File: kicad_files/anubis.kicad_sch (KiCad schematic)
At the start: 261 parts, among them J1 A1001WR-S-04P, J2 A1001WR-S-04P, J3 Conn_01x06, Q1 AO3401A, Q2 2N7002, Q3 DTC123JKAT146, Q4 DTC123JKAT146, Q5 DTC123JKAT146, Q6 DTC123JKAT146, SW1 K2-1187SQ-A4SW-06, SW10 MX Switch, SW100 MX Switch, SW101 MX Switch, SW102 MX Switch, SW103 MX Switch, SW104 MX Switch, SW11 MX Switch, SW12 MX Switch, SW13 MX Switch, SW14 MX Switch, SW15 MX Switch, SW16 MX Switch, SW17 MX Switch, SW18 MX Switch, SW19 MX Switch, SW2 MX Switch, SW20 MX Switch, SW21 MX Switch, SW22 MX Switch, SW23 MX Switch, SW24 MX Switch, SW25 MX Switch, SW26 MX Switch, SW27 MX Switch, SW28 MX Switch, SW29 MX Switch, SW3 MX Switch, SW30 MX Switch, SW31 MX Switch, SW32 MX Switch, SW33 MX Switch, SW34 MX Switch, SW35 MX Switch, SW36 MX Switch, SW37 MX Switch, SW38 MX Switch, SW39 MX Switch, SW4 MX Switch, SW40 MX Switch, SW41 MX Switch, SW42 MX Switch, SW43 MX Switch, SW44 MX Switch, SW45 MX Switch, SW46 MX Switch, SW47 MX Switch, SW48 MX Switch, SW49 MX Switch, SW5 MX Switch, SW50 MX Switch, SW51 MX Switch, SW52 MX Switch, SW53 MX Switch, SW54 MX Switch, SW55 MX Switch, SW56 MX Switch, SW57 MX Switch, SW58 MX Switch, SW59 MX Switch, SW6 MX Switch, SW60 MX Switch, SW61 MX Switch, SW62 MX Switch, SW63 MX Switch, SW64 MX Switch, SW65 MX Switch, SW66 MX Switch, SW67 MX Switch, SW68 MX Switch, SW69 MX Switch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

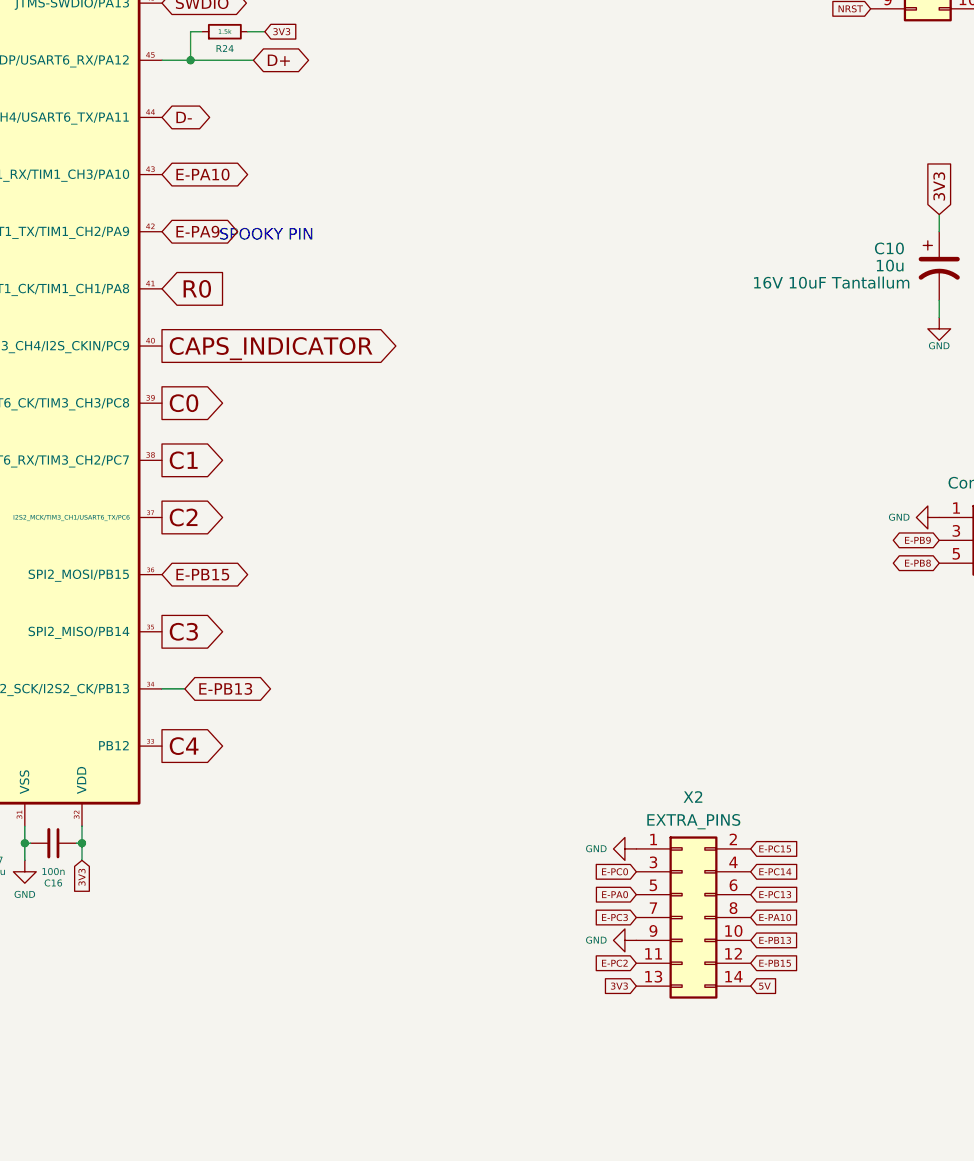
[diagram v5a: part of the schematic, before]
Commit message: Link LED_PWM pin to A10
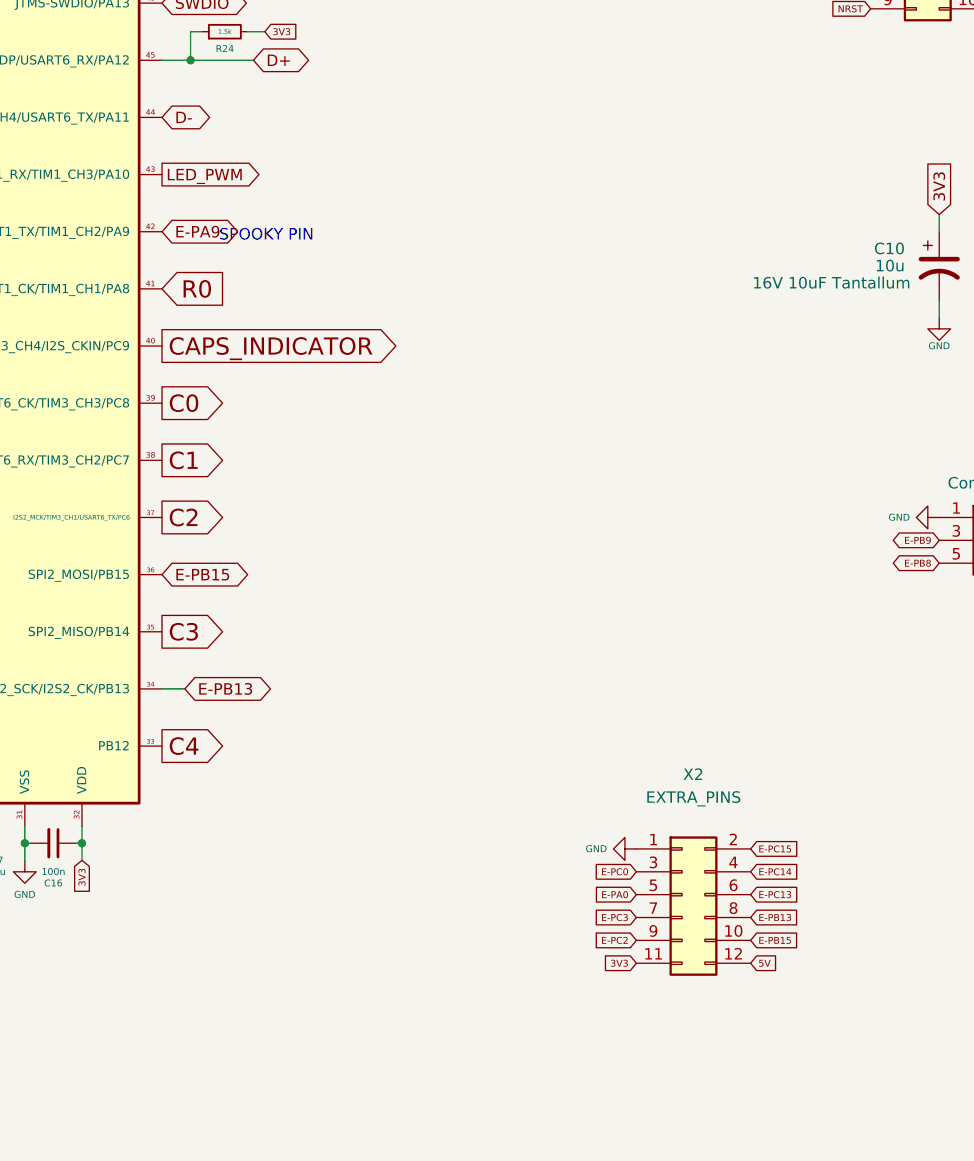
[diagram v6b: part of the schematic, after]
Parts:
- X2: footprint acheron_Connectors:PinHeader_2x7_P2.54mm_Vertical -> acheron_Connectors:PinHeader_2x6_P2.54mm_Vertical; symbol Connector_Generic:Conn_02x07_Odd_Even -> Connector_Generic:Conn_02x06_Odd_Even; now in the parts list
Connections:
- net 3V3: now also X2.11 (Pin_11); no longer X2.13 (Pin_13)
- net 5V: now also X2.12 (Pin_12); no longer X2.14 (Pin_14)
- net E-PB13: now also X2.8 (Pin_8); no longer X2.10 (Pin_10)
- net E-PB15: now also X2.10 (Pin_10); no longer X2.12 (Pin_12)
- net E-PC2: now also X2.9 (Pin_9); no longer X2.11 (Pin_11)
- net GND: no longer X2.9 (Pin_9)
- net LED_PWM: now also U4.43 (USART1_RX/TIM1_CH3/PA10)
- removed net E-PA10: U4.43 (USART1_RX/TIM1_CH3/PA10), X2.8 (Pin_8)
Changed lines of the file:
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@@
     (title "Anubis PCB schematic")
     (date "2022-05-21")
-    (rev "v1.0.0")
+    (rev "v1.0.1")
     (company "Designed by Gondolindrim")
     (comment 1 "For the AcheronProject")
@@
     )
   )
-  (global_label "E-PB15" (shape input) (at 755.65 432.435 0)
+  (global_label "E-PB15" (shape input) (at 755.65 429.895 0)
     (effects (font (size 0.762 0.762)) (justify left))
-    (property "Intersheet References" "${INTERSHEET_REFS}" (id 0) (at 759.2025 432.3874 0)
+    (property "Intersheet References" "${INTERSHEET_REFS}" (id 0) (at 759.2025 429.8474 0)
       (effects (font (size 0.762 0.762)) (justify left) hide)
     )
@@
     )
   )
-  (global_label "E-PA10" (shape input) (at 755.65 427.355 0)
-    (effects (font (size 0.762 0.762)) (justify left))
-    (property "Intersheet References" "${INTERSHEET_REFS}" (id 0) (at 759.2025 427.3074 0)
-      (effects (font (size 0.762 0.762)) (justify left) hide)
-    )
-  )
   (global_label "5V" (shape input) (at 287.02 157.48 180)
     (effects (font (size 0.762 0.762)) (justify right))
@@
     )
   )
-  (global_label "E-PB13" (shape input) (at 755.65 429.895 0)
+  (global_label "E-PB13" (shape input) (at 755.65 427.355 0)
     (effects (font (size 0.762 0.762)) (justify left))
-    (property "Intersheet References" "${INTERSHEET_REFS}" (id 0) (at 759.2025 429.8474 0)
+    (property "Intersheet References" "${INTERSHEET_REFS}" (id 0) (at 759.2025 427.3074 0)
       (effects (font (size 0.762 0.762)) (justify left) hide)
     )
@@
     )
   )
-  (global_label "E-PC2" (shape input) (at 742.95 432.435 180)
+  (global_label "E-PC2" (shape input) (at 742.95 429.895 180)
     (effects (font (size 0.762 0.762)) (justify right))
-    (property "Intersheet References" "${INTERSHEET_REFS}" (id 0) (at 739.3975 432.4826 0)
+    (property "Intersheet References" "${INTERSHEET_REFS}" (id 0) (at 739.3975 429.9426 0)
       (effects (font (size 0.762 0.762)) (justify right) hide)
     )
@@
     )
   )
-  (global_label "3V3" (shape input) (at 742.95 434.975 180)
+  (global_label "3V3" (shape input) (at 742.95 432.435 180)
     (effects (font (size 0.762 0.762)) (justify right))
-    (property "Intersheet References" "${INTERSHEET_REFS}" (id 0) (at 739.3975 435.0226 0)
+    (property "Intersheet References" "${INTERSHEET_REFS}" (id 0) (at 739.3975 432.4826 0)
       (effects (font (size 0.762 0.762)) (justify right) hide)
     )
@@
     )
   )
-  (global_label "E-PA10" (shape bidirectional) (at 690.245 344.805 0)
-    (effects (font (size 1.27 1.27)) (justify left))
-    (property "Intersheet References" "${INTERSHEET_REFS}" (id 0) (at 695.1376 344.7256 0)
-      (effects (font (size 1.27 1.27)) (justify left) hide)
-    )
-  )
   (global_label "C3" (shape output) (at 690.245 395.605 0)
     (effects (font (size 1.905 1.905)) (justify left))
@@
     )
   )
-  (global_label "5V" (shape input) (at 755.65 434.975 0)
+  (global_label "5V" (shape input) (at 755.65 432.435 0)
     (effects (font (size 0.762 0.762)) (justify left))
-    (property "Intersheet References" "${INTERSHEET_REFS}" (id 0) (at 759.2025 434.9274 0)
+    (property "Intersheet References" "${INTERSHEET_REFS}" (id 0) (at 759.2025 432.3874 0)
       (effects (font (size 0.762 0.762)) (justify left) hide)
     )
   )
+  (global_label "LED_PWM" (shape output) (at 690.245 344.805 0) (fields_autoplaced)
+    (effects (font (size 1.27 1.27)) (justify left))
+    (property "Intersheet References" "${INTERSHEET_REFS}" (id 0) (at 701.4362 344.7256 0)
+      (effects (font (size 1.27 1.27)) (justify left) hide)
+    )
+  )
   (global_label "XTAL_OUT" (shape input) (at 537.845 364.49 90)
     (effects (font (size 1.27 1.27)) (justify left))
@@
     (pin "K")
   )
-  (symbol (lib_id "Connector_Generic:Conn_02x07_Odd_Even") (at 748.03 427.355 0) (unit 1)
-    (in_bom no) (on_board yes)
-    (property "Reference" "X2" (id 0) (at 749.3 414.02 0))
-    (property "Value" "EXTRA_PINS" (id 1) (at 749.3 416.56 0))
-    (property "Footprint" "acheron_Connectors:PinHeader_2x7_P2.54mm_Vertical" (id 2) (at 748.03 427.355 0)
+  (symbol (lib_id "Connector_Generic:Conn_02x06_Odd_Even") (at 748.03 424.815 0) (unit 1)
+    (in_bom yes) (on_board yes)
+    (property "Reference" "X2" (id 0) (at 749.3 411.48 0))
+    (property "Value" "EXTRA_PINS" (id 1) (at 749.3 414.02 0))
+    (property "Footprint" "acheron_Connectors:PinHeader_2x6_P2.54mm_Vertical" (id 2) (at 748.03 424.815 0)
       (effects (font (size 1.27 1.27)) hide)
     )
-    (property "Datasheet" "~" (id 3) (at 748.03 427.355 0)
+    (property "Datasheet" "~" (id 3) (at 748.03 424.815 0)
       (effects (font (size 1.27 1.27)) hide)
     )
@@
     (pin "11")
     (pin "12")
-    (pin "13")
-    (pin "14")
     (pin "2")
     (pin "3")
@@
     (pin "2")
   )
-  (symbol (lib_id "power:GND") (at 742.95 429.895 270) (unit 1)
-    (in_bom yes) (on_board yes)
-    (property "Reference" "#PWR048" (id 0) (at 736.6 429.895 0)
-      (effects (font (size 1.27 1.27)) hide)
-    )
-    (property "Value" "GND" (id 1) (at 738.505 429.895 90)
-      (effects (font (size 0.762 0.762)))
-    )
-    (property "Footprint" "" (id 2) (at 742.95 429.895 0)
-      (effects (font (size 1.27 1.27)) hide)
-    )
-    (property "Datasheet" "" (id 3) (at 742.95 429.895 0)
-      (effects (font (size 1.27 1.27)) hide)
-    )
-    (pin "1")
-  )
   (symbol (lib_id "acheronSymbols:Mechanical_Switch") (at 138.43 446.405 0) (unit 1)
     (in_bom yes) (on_board yes)
@@
       (reference "#PWR047") (unit 1) (value "GND") (footprint "")
     )
-    (path "/870a80d5-078f-4720-9725-c73e0507bade"
-      (reference "#PWR048") (unit 1) (value "GND") (footprint "")
-    )
     (path "/6b3fe5ac-b56a-4aed-941a-05e686e6f2d5"
       (reference "C1") (unit 1) (value "100n") (footprint "Capacitor_SMD:C_0402_1005Metric")
@@
     )
     (path "/58373f7b-351f-4f64-a016-2ab8f90c3f61"
-      (reference "X2") (unit 1) (value "EXTRA_PINS") (footprint "acheron_Connectors:PinHeader_2x7_P2.54mm_Vertical")
+      (reference "X2") (unit 1) (value "EXTRA_PINS") (footprint "acheron_Connectors:PinHeader_2x6_P2.54mm_Vertical")
     )
     (path "/4c975a56-2d4a-4f14-81bb-55c4a4e1277f"

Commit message: Add label
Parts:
- added GR3: Anubis label, anubis_graphics:anubis_label, symbol Mechanical:MountingHole
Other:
- moved on the sheet: GR1, GR2, Q3, Q4, Q5, Q6, R13

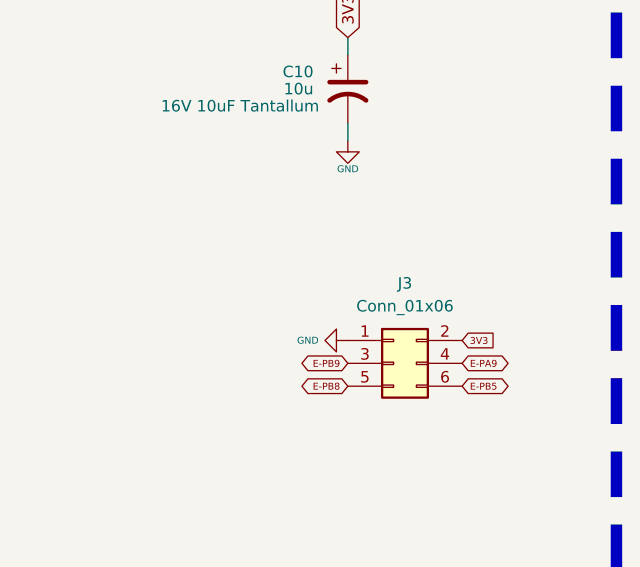
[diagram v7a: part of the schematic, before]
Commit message: Edit component metadata
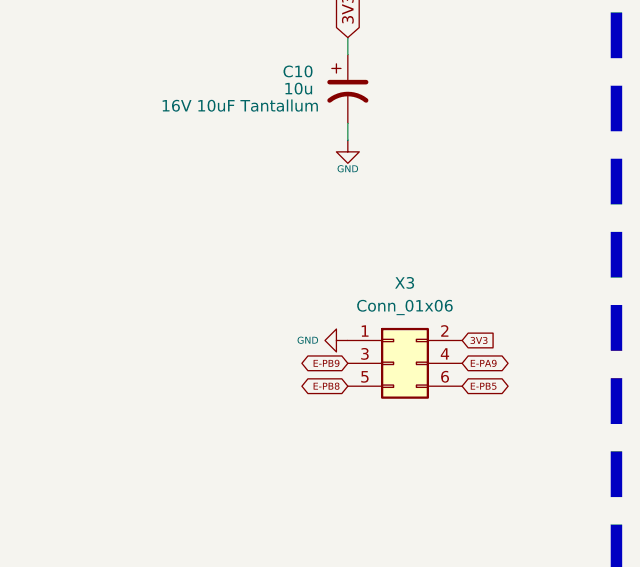
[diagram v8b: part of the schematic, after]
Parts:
- X2: now left out of the parts list
- renumbered J3 to X3
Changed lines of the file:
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@@
     (title "Anubis PCB schematic")
     (date "2022-05-21")
-    (rev "v1.0.2")
+    (rev "v1.0.3")
     (company "Designed by Gondolindrim")
     (comment 1 "For the AcheronProject")
@@
   (symbol (lib_id "Connector_Generic:Conn_02x03_Odd_Even") (at 781.685 385.445 0) (unit 1)
     (in_bom no) (on_board yes)
-    (property "Reference" "J3" (id 0) (at 782.955 376.555 0))
+    (property "Reference" "X3" (id 0) (at 782.955 376.555 0))
     (property "Value" "Conn_01x06" (id 1) (at 782.955 379.095 0))
     (property "Footprint" "acheron_Connectors:PinHeader_2x3_P2.54mm_Vertical" (id 2) (at 781.685 385.445 0)
@@
   )
   (symbol (lib_id "Connector_Generic:Conn_02x06_Odd_Even") (at 748.03 424.815 0) (unit 1)
-    (in_bom yes) (on_board yes)
+    (in_bom no) (on_board yes)
     (property "Reference" "X2" (id 0) (at 749.3 411.48 0))
     (property "Value" "EXTRA_PINS" (id 1) (at 749.3 414.02 0))
@@
       (reference "J2") (unit 1) (value "A1001WR-S-04P") (footprint "acheron_Connectors:SM04B-SRSS-TB(LF)(SN)_mounting-reliefs")
     )
-    (path "/3a146254-7ff6-44fa-bbbe-d41651ed1984"
-      (reference "J3") (unit 1) (value "Conn_01x06") (footprint "acheron_Connectors:PinHeader_2x3_P2.54mm_Vertical")
-    )
     (path "/576dd885-8cfb-4ef1-86b0-b4232178f99d"
       (reference "LED1") (unit 1) (value "LED") (footprint "acheron_Components:LED_THT_2.54mm")
@@
       (reference "X2") (unit 1) (value "EXTRA_PINS") (footprint "acheron_Connectors:PinHeader_2x6_P2.54mm_Vertical")
     )
+    (path "/3a146254-7ff6-44fa-bbbe-d41651ed1984"
+      (reference "X3") (unit 1) (value "Conn_01x06") (footprint "acheron_Connectors:PinHeader_2x3_P2.54mm_Vertical")
+    )
     (path "/4c975a56-2d4a-4f14-81bb-55c4a4e1277f"
